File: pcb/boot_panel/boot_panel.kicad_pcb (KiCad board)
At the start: 2 copper layers, 110 x 36 mm, 4 parts, among them J1 Conn_01x10_Socket

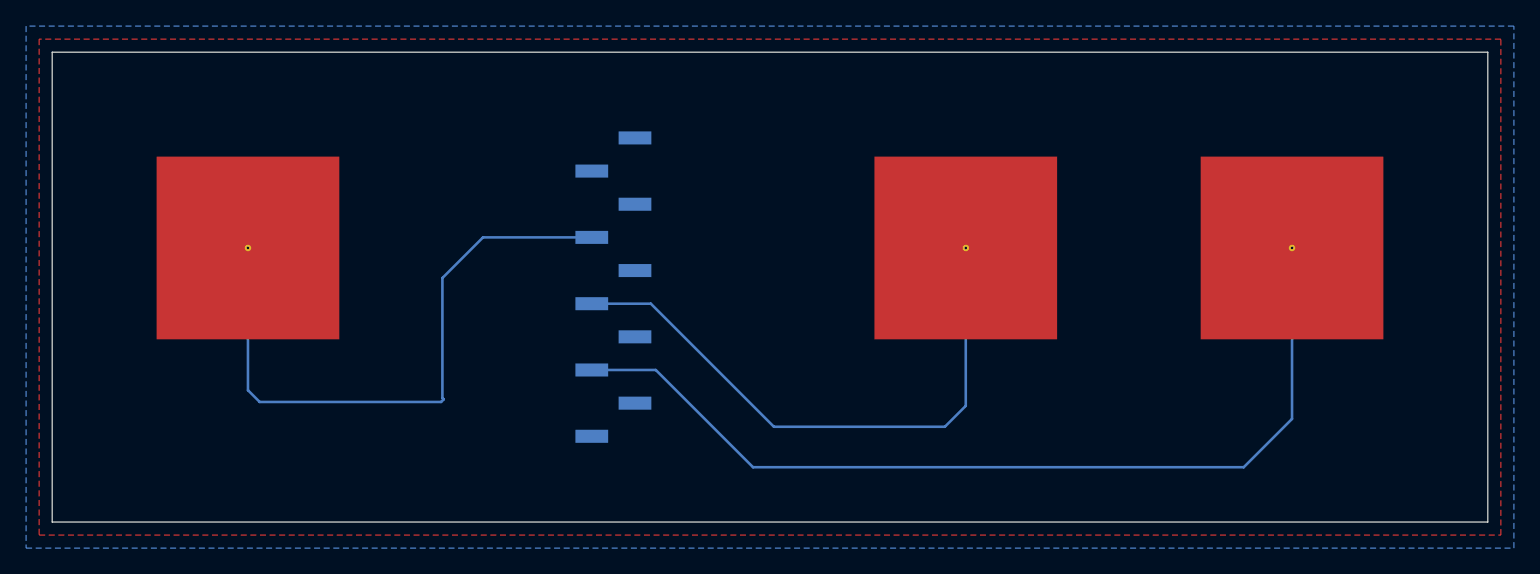
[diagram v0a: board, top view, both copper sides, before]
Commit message: move panel connector to fpc
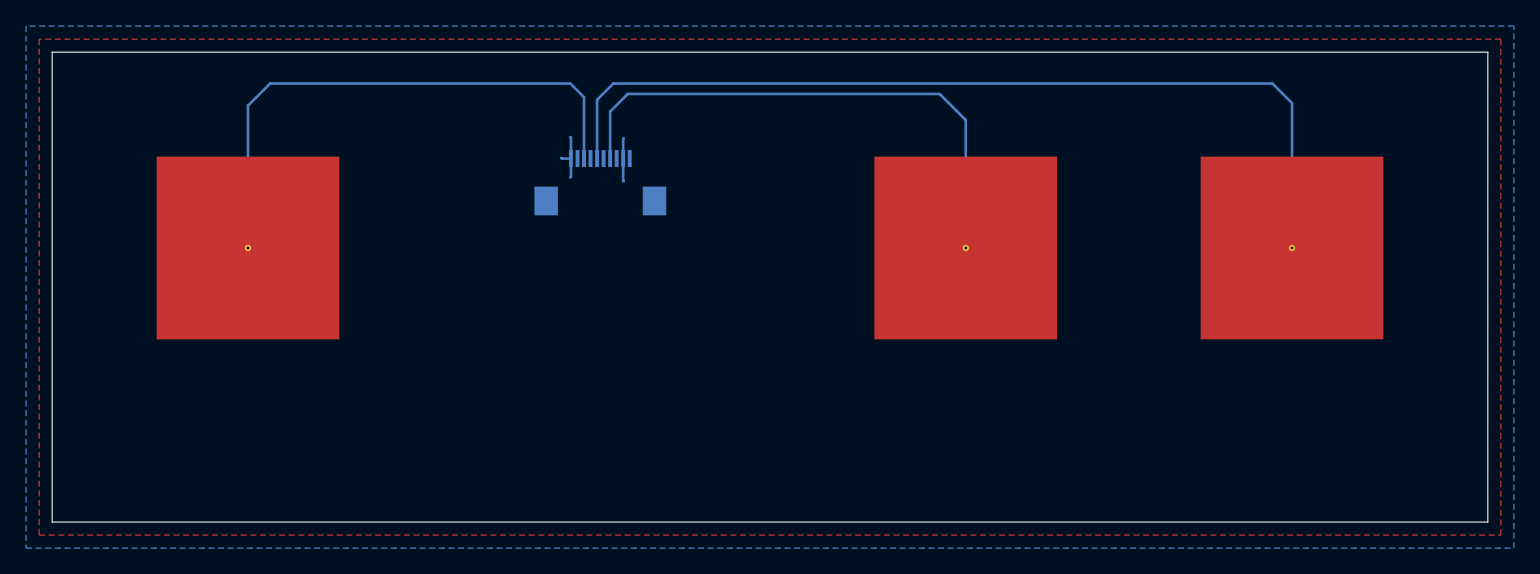
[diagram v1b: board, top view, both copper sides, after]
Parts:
- J1: footprint Connector_PinHeader_2.54mm:PinHeader_1x10_P2.54mm_Vertical_SMD_Pin1Left -> Connector_FFC-FPC:Hirose_FH12-10S-0.5SH_1x10-1MP_P0.50mm_Horizontal
- moved J1 8.06 mm to (142.0, 74.0)
- turned U1 to 180 degrees
- turned U2 to 180 degrees
- turned U3 to 180 degrees
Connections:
- U1 pad 1: Net-(J1-Pin_4) -> Net-(J1-Pin_8)
- U2 pad 1: Net-(J1-Pin_6) -> Net-(J1-Pin_4)
- U3 pad 1: Net-(J1-Pin_8) -> Net-(J1-Pin_6)
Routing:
- net Net-(J1-Pin_8): track 70.8 -> 41.9 mm
- net Net-(J1-Pin_6): track 44.8 -> 69.4 mm
- net GND: track 0.00 -> 7.25 mm
- net Net-(J1-Pin_4): track 47.9 -> 41.5 mm

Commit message: MOre layout
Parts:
- added H1: MountingHole, MountingHole:MountingHole_3.2mm_M3, F.Cu at (206.5, 67.5)
- added H2: MountingHole, MountingHole:MountingHole_3.2mm_M3, F.Cu at (206.5, 96.5)
- added H3: MountingHole, MountingHole:MountingHole_3.2mm_M3, F.Cu at (103.5, 96.5)
- added H4: MountingHole, MountingHole:MountingHole_3.2mm_M3, F.Cu at (103.5, 67.5)
- moved U1 3.00 mm to (118.0, 79.0)
- moved U2 3.00 mm to (167.0, 79.0)
- moved U3 3.00 mm to (192.0, 79.0)
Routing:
- net Net-(J1-Pin_6): track 69.4 -> 66.4 mm
- net Net-(J1-Pin_8): track 41.9 -> 39.0 mm
- net Net-(J1-Pin_4): track 41.5 -> 39.2 mm

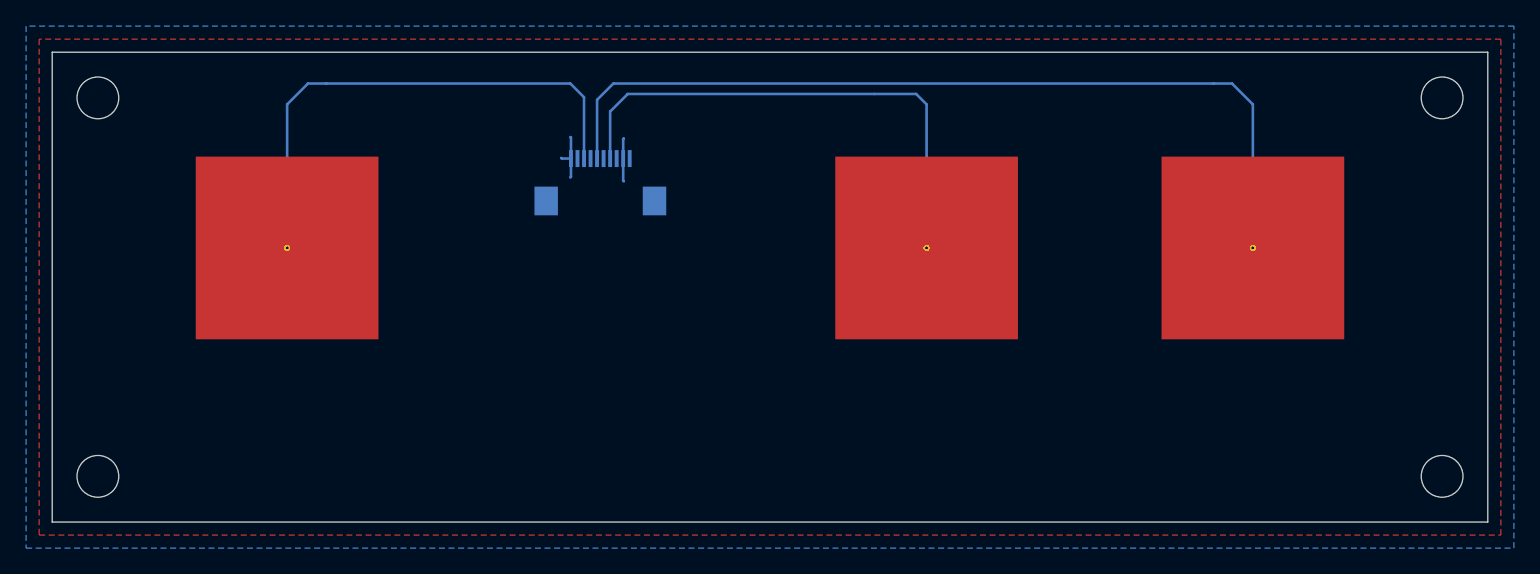
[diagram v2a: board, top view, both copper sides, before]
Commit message: move cap sense ic to front panel
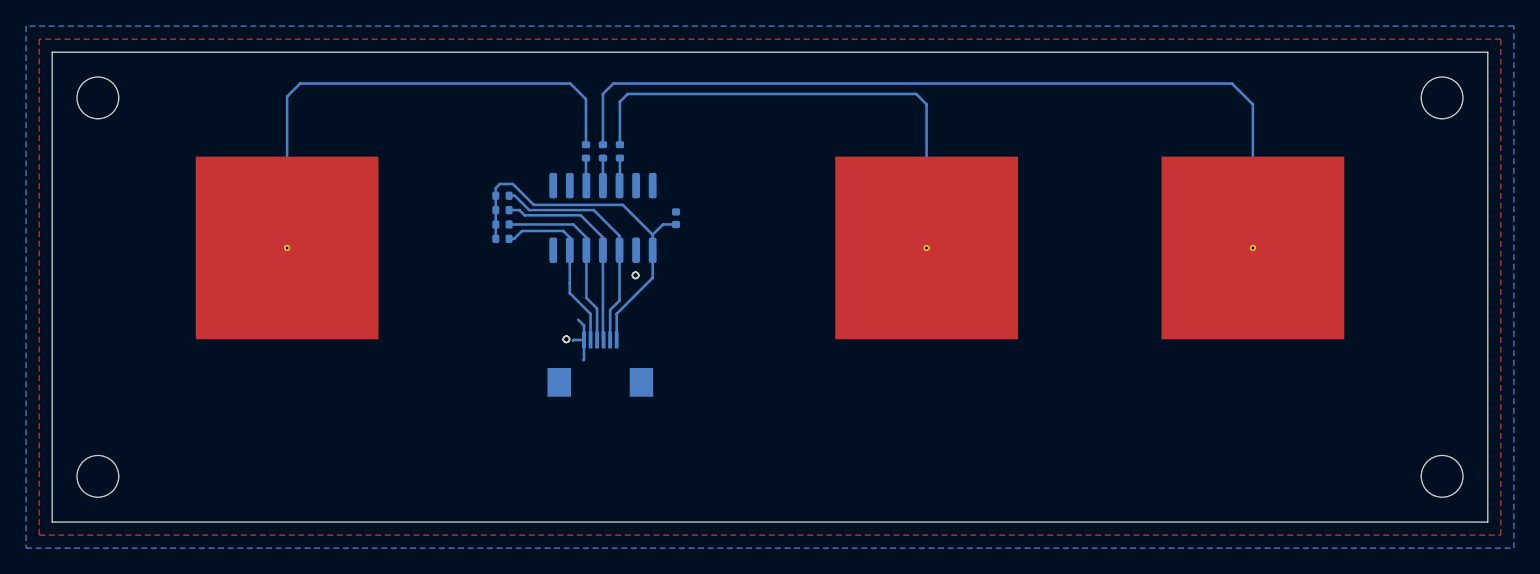
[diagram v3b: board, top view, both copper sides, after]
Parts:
- removed J1: Conn_01x10_Socket, Connector_FFC-FPC:Hirose_FH12-10S-0.5SH_1x10-1MP_P0.50mm_Horizontal
- added C1: 0.1u, Capacitor_SMD:C_0402_1005Metric, B.Cu at (147.8, 76.7)
- added J2: Conn_01x06_Pin, Connector_FFC-FPC:Hirose_FH12-6S-0.5SH_1x06-1MP_P0.50mm_Horizontal, B.Cu at (142.0, 87.9)
- added R1: 4.7k, Resistor_SMD:R_0402_1005Metric, B.Cu at (134.5, 75.0)
- added R2: 10k, Resistor_SMD:R_0402_1005Metric, B.Cu at (143.5, 71.6)
- added R3: 10k, Resistor_SMD:R_0402_1005Metric, B.Cu at (142.2, 71.6)
- added R4: 10k, Resistor_SMD:R_0402_1005Metric, B.Cu at (140.9, 71.6)
- added R5: 4.7k, Resistor_SMD:R_0402_1005Metric, B.Cu at (134.5, 78.3)
- added R6: 10k, Resistor_SMD:R_0402_1005Metric, B.Cu at (134.5, 76.1)
- added R7: 10k, Resistor_SMD:R_0402_1005Metric, B.Cu at (134.5, 77.2)
- added U4: AT42QT1070-S, Package_SO:SOIC-14_3.9x8.7mm_P1.27mm, B.Cu at (142.2, 76.7)
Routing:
- net +3V3: track 0.00 -> 29.2 mm
- net /SDA: track 0.00 -> 18.0 mm
- net /RES: track 0.00 -> 15.9 mm
- net /CHG: track 0.00 -> 14.5 mm
- net /SCL: track 0.00 -> 13.6 mm
- net GND: track 7.25 -> 4.18 mm, vias 0 -> 4
- net Net-(U4-KEY3): track 0.00 -> 2.13 mm
- net Net-(U4-KEY1): track 0.00 -> 2.13 mm
- net Net-(U4-KEY2): track 0.00 -> 2.11 mm
- net Net-(U2-PAD): track 39.2 -> 37.8 mm
- net Net-(U3-PAD): track 66.4 -> 65.1 mm
- net Net-(U1-PAD): track 39.0 -> 38.4 mm

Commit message: More layout
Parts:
- C1: footprint Capacitor_SMD:C_0402_1005Metric -> Capacitor_SMD:C_0603_1608Metric_Pad1.08x0.95mm_HandSolder
- R1, R2, R3, R4, R5, R6, R7: footprint Resistor_SMD:R_0402_1005Metric -> Resistor_SMD:R_0603_1608Metric_Pad0.98x0.95mm_HandSolder
- moved R4 1.28 mm to (140.2, 70.5)
- moved R2 1.21 mm to (144.0, 70.5)
- moved R3 1.10 mm to (142.2, 70.5)
- moved R1 1.00 mm to (134.5, 74.0)
- moved R5 0.95 mm to (134.5, 79.2)
- moved R6 0.35 mm to (134.5, 75.8)
- moved R7 0.30 mm to (134.5, 77.5)
- moved C1 0.20 mm to (148.0, 76.8)
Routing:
- net +3V3: track 29.2 -> 32.1 mm
- net Net-(U2-PAD): track 37.8 -> 36.0 mm
- net Net-(U1-PAD): track 38.4 -> 36.6 mm
- net Net-(U3-PAD): track 65.1 -> 63.6 mm
- net Net-(U4-KEY3): track 2.13 -> 3.14 mm
- net Net-(U4-KEY1): track 2.13 -> 3.07 mm
- net Net-(U4-KEY2): track 2.11 -> 2.81 mm
